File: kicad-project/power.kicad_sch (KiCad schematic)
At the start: 22 parts

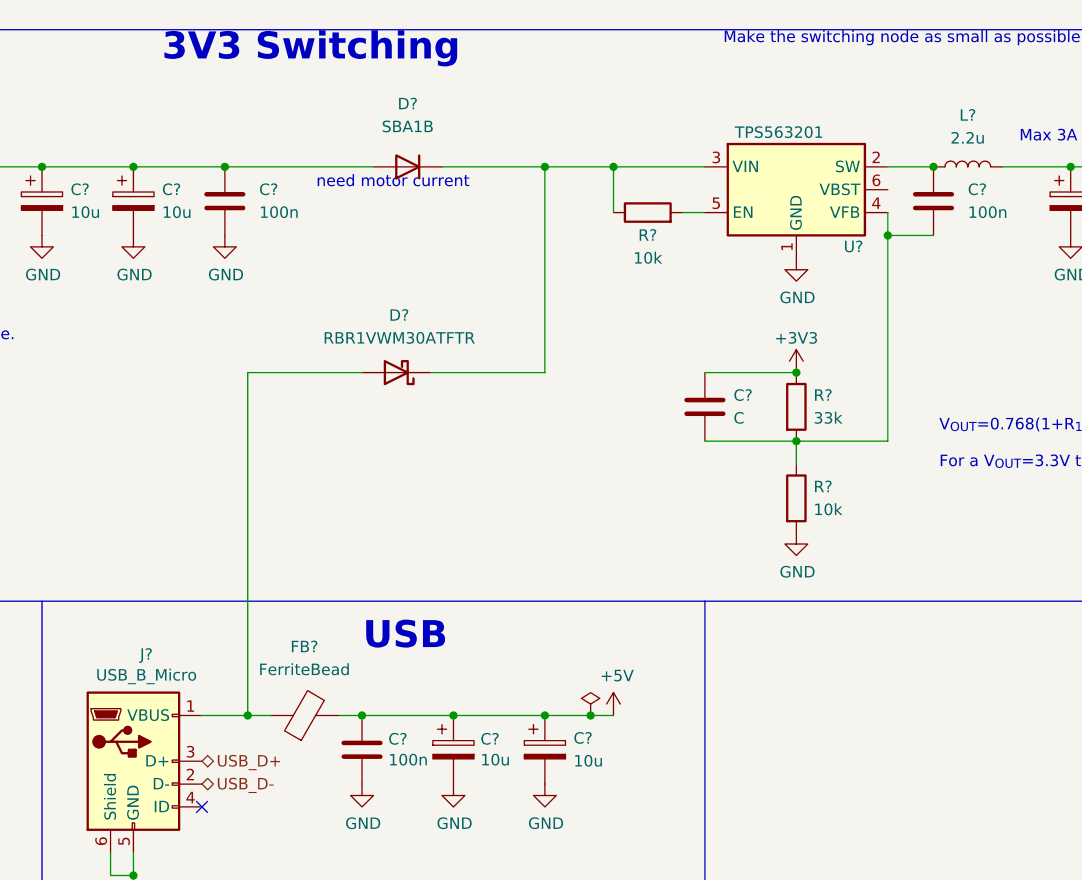
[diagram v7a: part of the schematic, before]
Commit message: hw: set grid to 50 mils and missing labels
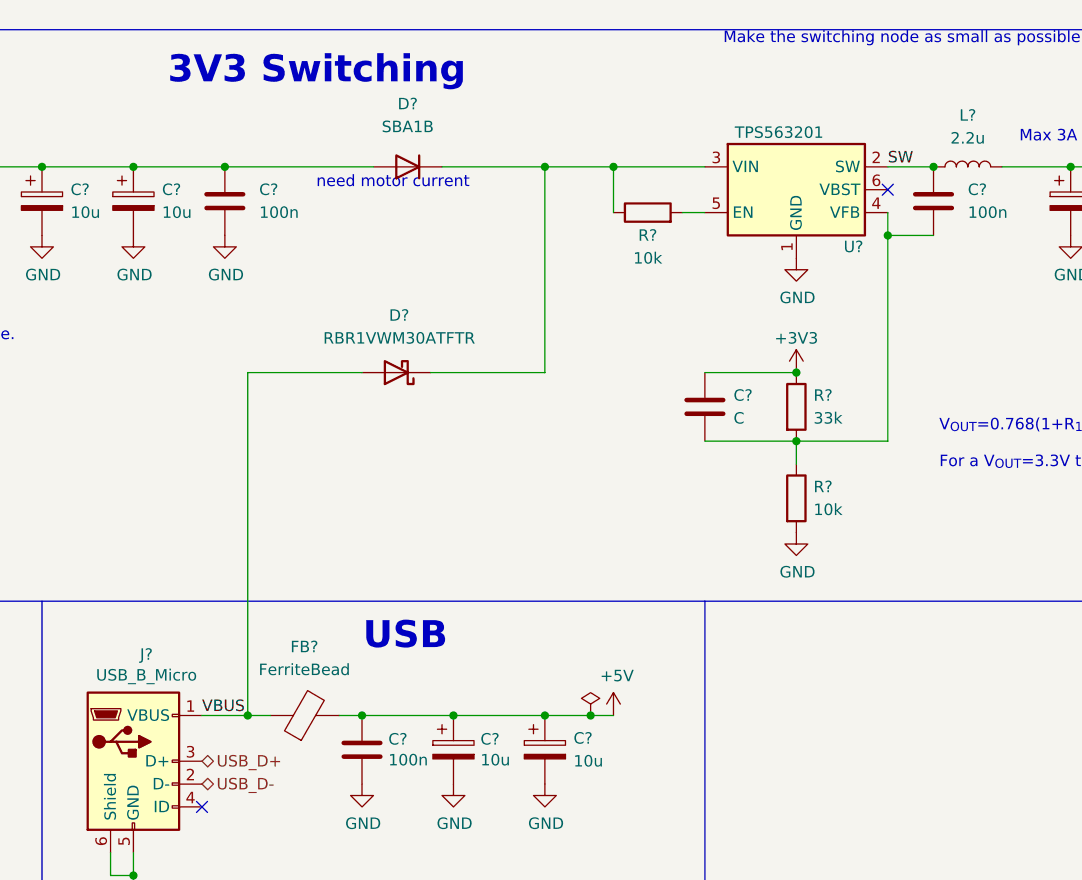
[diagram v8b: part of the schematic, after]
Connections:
- net VBUS: now reaches D?.2 (A), FB?.1, J?.1 (VBUS)
- net SW: now reaches C?.1, L?.1, U?.2 (SW)
- no-connect marks 1 -> 2
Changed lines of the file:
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@@
   (junction (at 172.72 38.1) (diameter 0) (color 0 0 0 0)
   )
+  (no_connect (at 172.72 33.02))
   (no_connect (at 96.52 101.6))
   (wire (pts (xy 172.72 38.1) (xy 172.72 60.96))
@@
     (effects (font (size 1.27 1.27)) (justify left bottom))
   )
-  (text "3V3 Switching" (at 92.075 19.05 0)
+  (text "3V3 Switching" (at 92.71 21.59 0)
     (effects (font (size 3 3) (thickness 0.6) bold) (justify left bottom))
   )
@@
     (effects (font (size 1.27 1.27)) (justify left bottom))
   )
+  (label "SW" (at 172.72 30.48 0)
+    (effects (font (size 1.27 1.27)) (justify left bottom))
+  )
+  (label "VBUS" (at 96.52 91.44 0)
+    (effects (font (size 1.27 1.27)) (justify left bottom))
+  )
